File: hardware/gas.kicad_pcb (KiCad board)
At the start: 2 copper layers, 65 x 30 mm, 29 parts, among them P1 CON-SENSOR2, P2 DEBUG, P3 BOOT, P4 Gas Sensor, U1 XMC1300, U2 DRILL, U3 DRILL, U4 DRILL, U5 DRILL

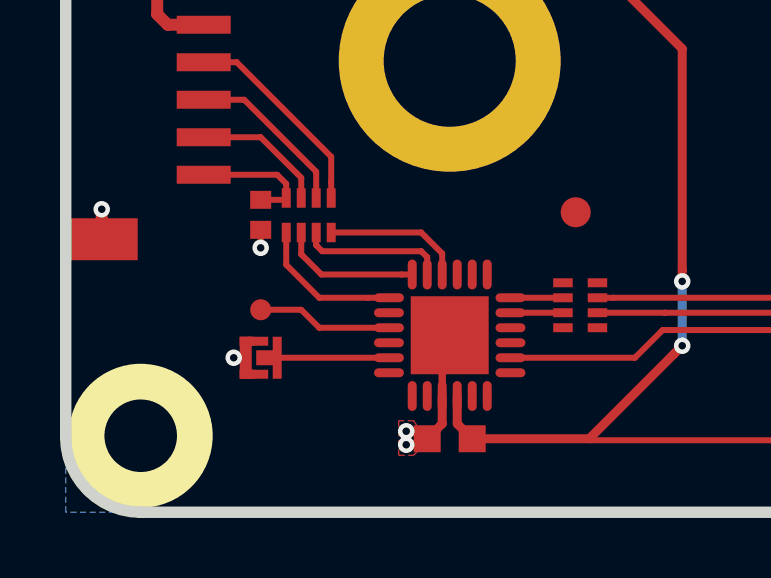
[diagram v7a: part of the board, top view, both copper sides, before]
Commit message: changed debugpin
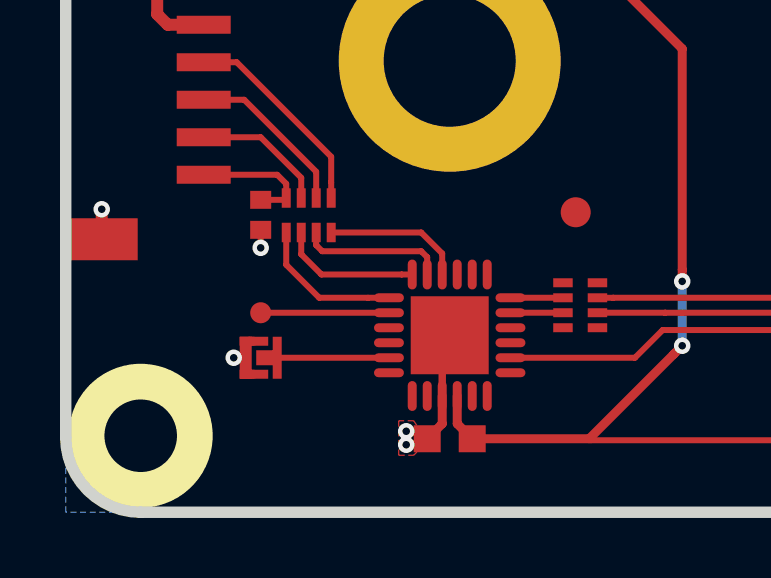
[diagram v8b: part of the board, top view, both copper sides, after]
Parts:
- moved P2 0.10 mm to (126.5, 103.3)
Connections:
- U1 pad 2: Net-(U1-Pad2) -> Net-(P2-Pad1)
- U1 pad 3: Net-(P2-Pad1) -> Net-(U1-Pad3)
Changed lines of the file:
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@@
     (thickness 1.6)
     (drawings 15)
-    (tracks 147)
+    (tracks 145)
     (zones 0)
     (modules 29)
@@
     (pad_drill 0.6)
     (pad_to_mask_clearance 0)
+    (solder_mask_min_width 0.25)
     (aux_axis_origin 120 80)
     (grid_origin 120 80)
@@
   (net 26 "Net-(RP2-Pad4)")
   (net 27 "Net-(RP2-Pad1)")
-  (net 28 "Net-(U1-Pad2)")
-  (net 29 "Net-(U1-Pad4)")
-  (net 30 "Net-(U1-Pad6)")
-  (net 31 "Net-(U1-Pad7)")
-  (net 32 "Net-(U1-Pad8)")
-  (net 33 "Net-(U1-Pad11)")
-  (net 34 "Net-(U1-Pad12)")
-  (net 35 "Net-(U1-Pad13)")
-  (net 36 "Net-(U1-Pad15)")
-  (net 37 "Net-(U1-Pad16)")
-  (net 38 "Net-(U1-Pad19)")
-  (net 39 "Net-(U1-Pad20)")
-  (net 40 "Net-(U1-Pad21)")
+  (net 28 "Net-(U1-Pad4)")
+  (net 29 "Net-(U1-Pad6)")
+  (net 30 "Net-(U1-Pad7)")
+  (net 31 "Net-(U1-Pad8)")
+  (net 32 "Net-(U1-Pad11)")
+  (net 33 "Net-(U1-Pad12)")
+  (net 34 "Net-(U1-Pad13)")
+  (net 35 "Net-(U1-Pad15)")
+  (net 36 "Net-(U1-Pad16)")
+  (net 37 "Net-(U1-Pad19)")
+  (net 38 "Net-(U1-Pad20)")
+  (net 39 "Net-(U1-Pad21)")
+  (net 40 "Net-(U1-Pad3)")
   (net_class Default "Dies ist die voreingestellte Netzklasse."
     (clearance 0.149)
@@
     (add_net "Net-(U1-Pad16)")
     (add_net "Net-(U1-Pad19)")
-    (add_net "Net-(U1-Pad2)")
     (add_net "Net-(U1-Pad20)")
     (add_net "Net-(U1-Pad21)")
+    (add_net "Net-(U1-Pad3)")
     (add_net "Net-(U1-Pad4)")
     (add_net "Net-(U1-Pad6)")
@@
   )
   (module kicad-libraries:DEBUG_PAD (layer F.Cu)
-    (at 126.5 103.25 270)
+    (at 126.5 103.35 270)
     (fp_text reference P2 (at 0 0.175 270) (layer F.Fab)
       (effects (font (size 0.15 0.15) (thickness 0.0375)))
@@
       (net 9 S-MISO))
     (pad 2 smd oval (at -2.025 -0.75) (size 1 0.3) (layers F.Cu F.Paste F.Mask)
-      (net 28 "Net-(U1-Pad2)"))
+      (net 18 "Net-(P2-Pad1)"))
     (pad 3 smd oval (at -2.025 -0.25) (size 1 0.3) (layers F.Cu F.Paste F.Mask)
-      (net 18 "Net-(P2-Pad1)"))
+      (net 40 "Net-(U1-Pad3)"))
     (pad 4 smd oval (at -2.025 0.25) (size 1 0.3) (layers F.Cu F.Paste F.Mask)
-      (net 29 "Net-(U1-Pad4)"))
+      (net 28 "Net-(U1-Pad4)"))
     (pad 5 smd oval (at -2.025 0.75) (size 1 0.3) (layers F.Cu F.Paste F.Mask)
       (net 19 "Net-(P3-Pad2)"))
     (pad 6 smd oval (at -2.025 1.25) (size 1 0.3) (layers F.Cu F.Paste F.Mask)
-      (net 30 "Net-(U1-Pad6)"))
+      (net 29 "Net-(U1-Pad6)"))
     (pad 7 smd oval (at -1.25 2.025 90) (size 1 0.3) (layers F.Cu F.Paste F.Mask)
-      (net 31 "Net-(U1-Pad7)"))
+      (net 30 "Net-(U1-Pad7)"))
     (pad 8 smd oval (at -0.75 2.025 90) (size 1 0.3) (layers F.Cu F.Paste F.Mask)
-      (net 32 "Net-(U1-Pad8)"))
+      (net 31 "Net-(U1-Pad8)"))
     (pad 9 smd oval (at -0.25 2.025 90) (size 1 0.3) (layers F.Cu F.Paste F.Mask)
       (net 2 GND))
@@
       (net 1 VCC))
     (pad 11 smd oval (at 0.75 2.025 90) (size 1 0.3) (layers F.Cu F.Paste F.Mask)
-      (net 33 "Net-(U1-Pad11)"))
+      (net 32 "Net-(U1-Pad11)"))
     (pad 12 smd oval (at 1.25 2.025 90) (size 1 0.3) (layers F.Cu F.Paste F.Mask)
-      (net 34 "Net-(U1-Pad12)"))
+      (net 33 "Net-(U1-Pad12)"))
     (pad 13 smd oval (at 2.025 1.25) (size 1 0.3) (layers F.Cu F.Paste F.Mask)
-      (net 35 "Net-(U1-Pad13)"))
+      (net 34 "Net-(U1-Pad13)"))
     (pad 14 smd oval (at 2.025 0.75) (size 1 0.3) (layers F.Cu F.Paste F.Mask)
       (net 8 "Net-(R1-Pad1)"))
     (pad 15 smd oval (at 2.025 0.25) (size 1 0.3) (layers F.Cu F.Paste F.Mask)
-      (net 36 "Net-(U1-Pad15)"))
+      (net 35 "Net-(U1-Pad15)"))
     (pad 16 smd oval (at 2.025 -0.25) (size 1 0.3) (layers F.Cu F.Paste F.Mask)
-      (net 37 "Net-(U1-Pad16)"))
+      (net 36 "Net-(U1-Pad16)"))
     (pad 17 smd oval (at 2.025 -0.75) (size 1 0.3) (layers F.Cu F.Paste F.Mask)
       (net 13 GS_TX))
@@
       (net 14 GS_RX))
     (pad 19 smd oval (at 1.25 -2.025 90) (size 1 0.3) (layers F.Cu F.Paste F.Mask)
-      (net 38 "Net-(U1-Pad19)"))
+      (net 37 "Net-(U1-Pad19)"))
     (pad 20 smd oval (at 0.75 -2.025 90) (size 1 0.3) (layers F.Cu F.Paste F.Mask)
-      (net 39 "Net-(U1-Pad20)"))
+      (net 38 "Net-(U1-Pad20)"))
     (pad 21 smd oval (at 0.25 -2.025 90) (size 1 0.3) (layers F.Cu F.Paste F.Mask)
-      (net 40 "Net-(U1-Pad21)"))
+      (net 39 "Net-(U1-Pad21)"))
     (pad 22 smd oval (at -0.25 -2.025 90) (size 1 0.3) (layers F.Cu F.Paste F.Mask)
       (net 12 S-CS))
@@
   (segment (start 127.05 98.75) (end 127.3507 99.0507) (width 0.2) (layer F.Cu) (net 15))
   (segment (start 153.3 108.45) (end 154.8499 108.45) (width 0.2) (layer F.Cu) (net 16))
-  (segment (start 127.85 103.25) (end 126.5 103.25) (width 0.2) (layer F.Cu) (net 18))
-  (segment (start 130.775 103.85) (end 128.45 103.85) (width 0.2) (layer F.Cu) (net 18))
-  (segment (start 128.45 103.85) (end 127.85 103.25) (width 0.2) (layer F.Cu) (net 18))
+  (segment (start 130.775 103.35) (end 126.45 103.35) (width 0.2) (layer F.Cu) (net 18))
   (segment (start 126.65 104.85) (end 130.775 104.85) (width 0.2) (layer F.Cu) (net 19))
   (zone (net 2) (net_name GND) (layer B.Cu) (hatch edge 0.508)
